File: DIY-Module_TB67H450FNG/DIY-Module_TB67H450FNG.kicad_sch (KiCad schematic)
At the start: 6 parts, among them IC1 Motor_A, IC2 Motor_B, J1 Conn_01x07_Pin, J2 Conn_01x07_Pin

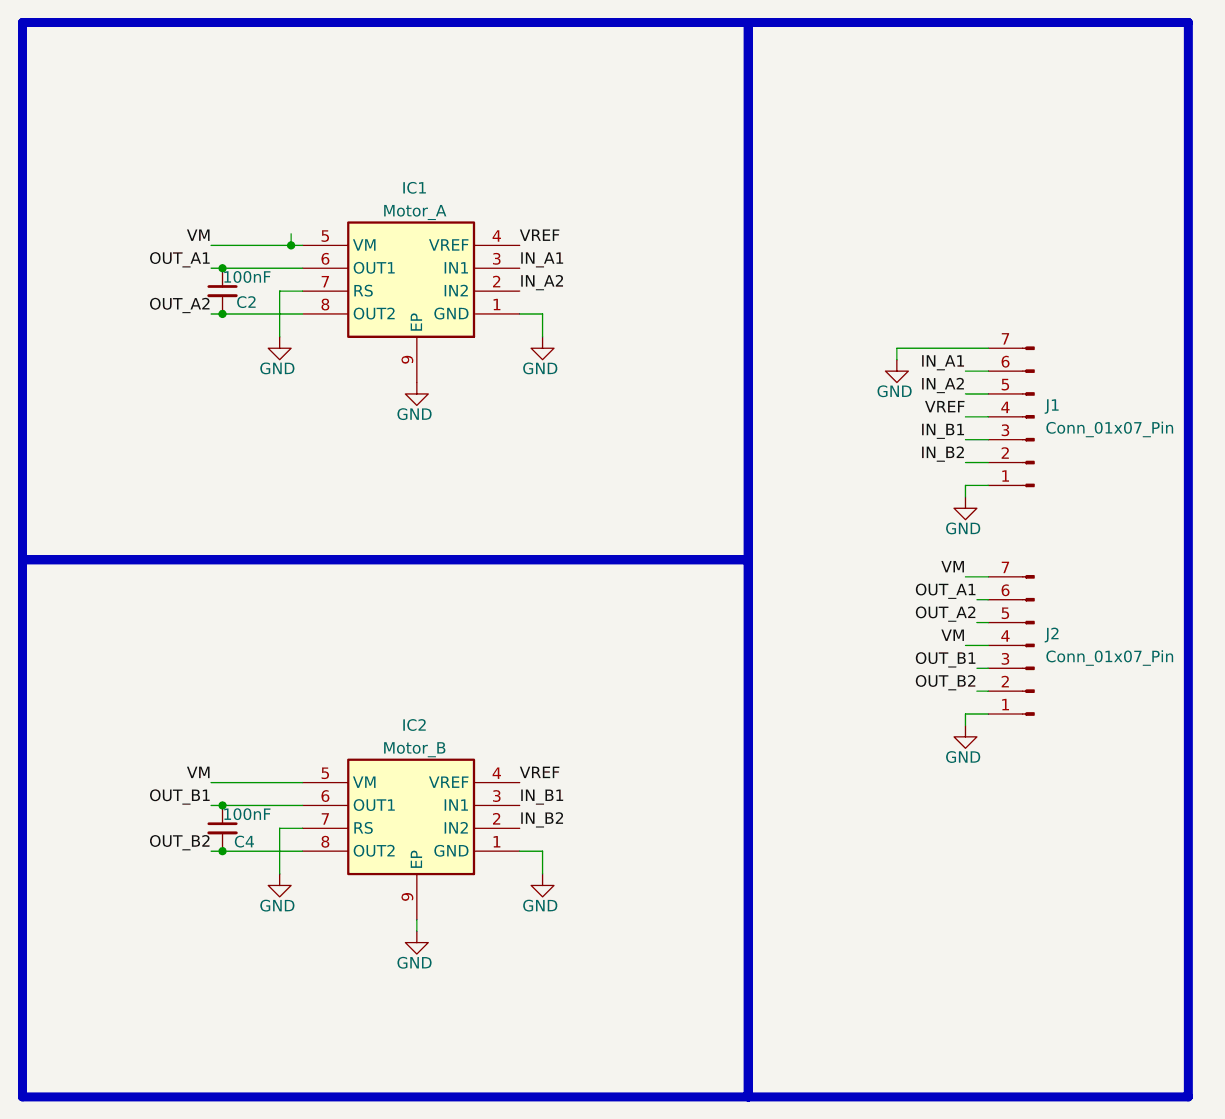
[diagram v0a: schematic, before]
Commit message: Removed capacitors & update README.md
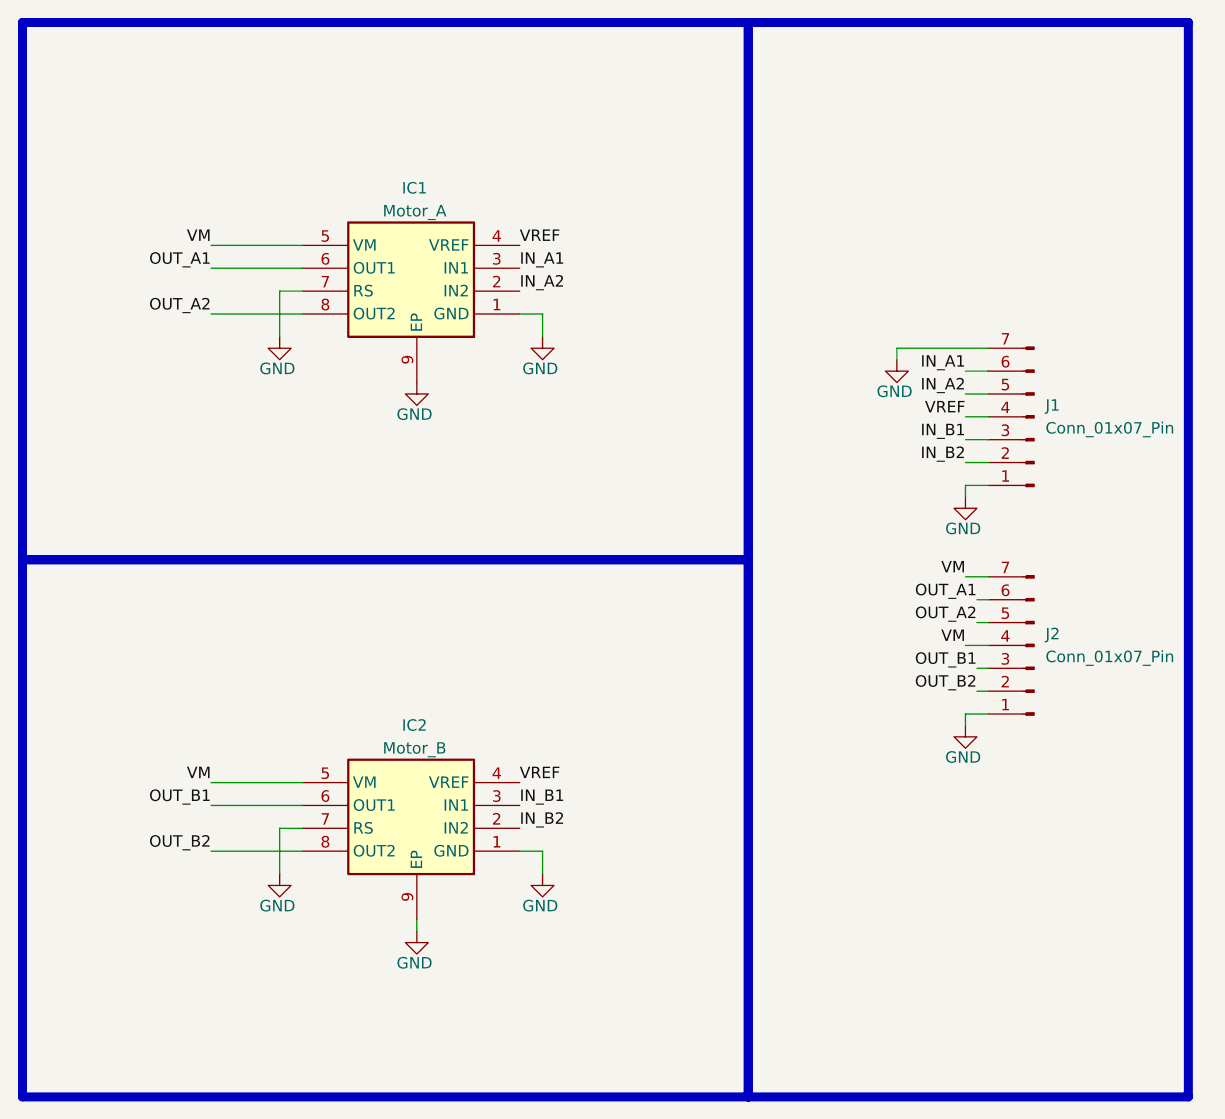
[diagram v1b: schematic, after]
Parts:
- removed C2, C4: 100nF, Capacitor_SMD:C_0805_2012Metric_Pad1.18x1.45mm_HandSolder, symbol Device:C_Small
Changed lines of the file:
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@@
 	(generator_version "8.0")
 	(paper "A4")
-	(junction
-		(at 38.1 41.91)
-		(diameter 0)
-		(color 0 0 0 0)
-	)
-	(junction
-		(at 38.1 101.6)
-		(diameter 0)
-		(color 0 0 0 0)
-	)
-	(junction
-		(at 38.1 46.99)
-		(diameter 0)
-		(color 0 0 0 0)
-	)
-	(junction
-		(at 45.72 39.37)
-		(diameter 0)
-		(color 0 0 0 0)
-	)
-	(junction
-		(at 38.1 106.68)
-		(diameter 0)
-		(color 0 0 0 0)
-	)
 	(wire
 		(pts
@@
 	(wire
 		(pts
-			(xy 38.1 106.68) (xy 46.99 106.68)
+			(xy 36.83 106.68) (xy 46.99 106.68)
 		)
 		(stroke
@@
 	(wire
 		(pts
-			(xy 36.83 46.99) (xy 38.1 46.99)
-		)
-		(stroke
-			(width 0)
-			(type default)
-		)
-	)
-	(wire
-		(pts
 			(xy 120.65 58.42) (xy 123.19 58.42)
 		)
@@
 	(wire
 		(pts
-			(xy 38.1 46.99) (xy 46.99 46.99)
+			(xy 36.83 46.99) (xy 46.99 46.99)
 		)
 		(stroke
@@
 	(wire
 		(pts
-			(xy 36.83 106.68) (xy 38.1 106.68)
-		)
-		(stroke
-			(width 0)
-			(type default)
-		)
-	)
-	(wire
-		(pts
-			(xy 36.83 101.6) (xy 38.1 101.6)
-		)
-		(stroke
-			(width 0)
-			(type default)
-		)
-	)
-	(wire
-		(pts
 			(xy 59.69 114.3) (xy 59.69 115.57)
 		)
@@
 	(wire
 		(pts
-			(xy 38.1 41.91) (xy 46.99 41.91)
+			(xy 36.83 41.91) (xy 46.99 41.91)
 		)
 		(stroke
@@
 	(wire
 		(pts
-			(xy 36.83 39.37) (xy 45.72 39.37)
-		)
-		(stroke
-			(width 0)
-			(type default)
-		)
-	)
-	(wire
-		(pts
-			(xy 38.1 101.6) (xy 46.99 101.6)
+			(xy 36.83 39.37) (xy 46.99 39.37)
+		)
+		(stroke
+			(width 0)
+			(type default)
+		)
+	)
+	(wire
+		(pts
+			(xy 36.83 101.6) (xy 46.99 101.6)
 		)
 		(stroke
@@
 	(wire
 		(pts
-			(xy 45.72 39.37) (xy 46.99 39.37)
-		)
-		(stroke
-			(width 0)
-			(type default)
-		)
-	)
-	(wire
-		(pts
-			(xy 36.83 41.91) (xy 38.1 41.91)
-		)
-		(stroke
-			(width 0)
-			(type default)
-		)
-	)
-	(wire
-		(pts
 			(xy 120.65 53.34) (xy 123.19 53.34)
 		)
@@
 		(pts
 			(xy 73.66 109.22) (xy 73.66 106.68)
-		)
-		(stroke
-			(width 0)
-			(type default)
-		)
-	)
-	(wire
-		(pts
-			(xy 45.72 39.37) (xy 45.72 38.1)
 		)
 		(stroke
@@
 	)
 	(symbol
-		(lib_id "Device:C_Small")
-		(at 38.1 44.45 0)
-		(unit 1)
-		(exclude_from_sim no)
-		(in_bom yes)
-		(on_board yes)
-		(dnp no)
-		(property "Reference" "C2"
-			(at 39.624 45.72 0)
-			(effects
-				(font
-					(size 1.27 1.27)
-				)
-				(justify left)
-			)
-		)
-		(property "Value" "100nF"
-			(at 38.1 42.926 0)
-			(effects
-				(font
-					(size 1.27 1.27)
-				)
-				(justify left)
-			)
-		)
-		(property "Footprint" "Capacitor_SMD:C_0805_2012Metric_Pad1.18x1.45mm_HandSolder"
-			(at 38.1 44.45 0)
-			(effects
-				(font
-					(size 1.27 1.27)
-				)
-				(hide yes)
-			)
-		)
-		(property "Datasheet" "~"
-			(at 38.1 44.45 0)
-			(effects
-				(font
-					(size 1.27 1.27)
-				)
-				(hide yes)
-			)
-		)
-		(property "Description" "Unpolarized capacitor, small symbol"
-			(at 38.1 44.45 0)
-			(effects
-				(font
-					(size 1.27 1.27)
-				)
-				(hide yes)
-			)
-		)
-		(pin "1"
-		)
-		(pin "2"
-		)
-		(instances
-			(project "driver_dual_TB67H450"
-				(path "/f2a6858f-f9d0-41c3-b1f2-5194c6bbfd5f"
-					(reference "C2")
-					(unit 1)
-				)
-			)
-		)
-	)
-	(symbol
 		(lib_id "power:GND")
 		(at 73.66 49.53 0)
@@
 					(unit 1)
 				)
-			)
-		)
-	)
-	(symbol
-		(lib_id "Device:C_Small")
-		(at 38.1 104.14 0)
-		(unit 1)
-		(exclude_from_sim no)
-		(in_bom yes)
-		(on_board yes)
-		(dnp no)
-		(property "Reference" "C4"
-			(at 39.37 105.664 0)
-			(effects
-				(font
-					(size 1.27 1.27)
-				)
-				(justify left)
-			)
-		)
-		(property "Value" "100nF"
-			(at 38.1 102.616 0)
-			(effects
-				(font
-					(size 1.27 1.27)
-				)
-				(justify left)
-			)
-		)
-		(property "Footprint" "Capacitor_SMD:C_0805_2012Metric_Pad1.18x1.45mm_HandSolder"
-			(at 38.1 104.14 0)
-			(effects
-				(font
-					(size 1.27 1.27)
-				)
-				(hide yes)
-			)
-		)
-		(property "Datasheet" "~"
-			(at 38.1 104.14 0)
-			(effects
-				(font
-					(size 1.27 1.27)
-				)
-				(hide yes)
-			)
-		)
-		(property "Description" "Unpolarized capacitor, small symbol"
-			(at 38.1 104.14 0)
-			(effects
-				(font
-					(size 1.27 1.27)
-				)
-				(hide yes)
-			)
-		)
-		(pin "1"
-		)
-		(pin "2"
-		)
-		(instances
-			(project "driver_dual_TB67H450"
-				(path "/f2a6858f-f9d0-41c3-b1f2-5194c6bbfd5f"
-					(reference "C4")
-					(unit 1)
-				)
